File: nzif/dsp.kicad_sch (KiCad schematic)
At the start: 64 parts, among them Q501 STD2805T4, SW501 SW_SPST, SW502 SW_Push, U501 ADAU1467WBCPZ300, U502 25AA1024-I/MF, U503 ADM811TARTZ-REEL7

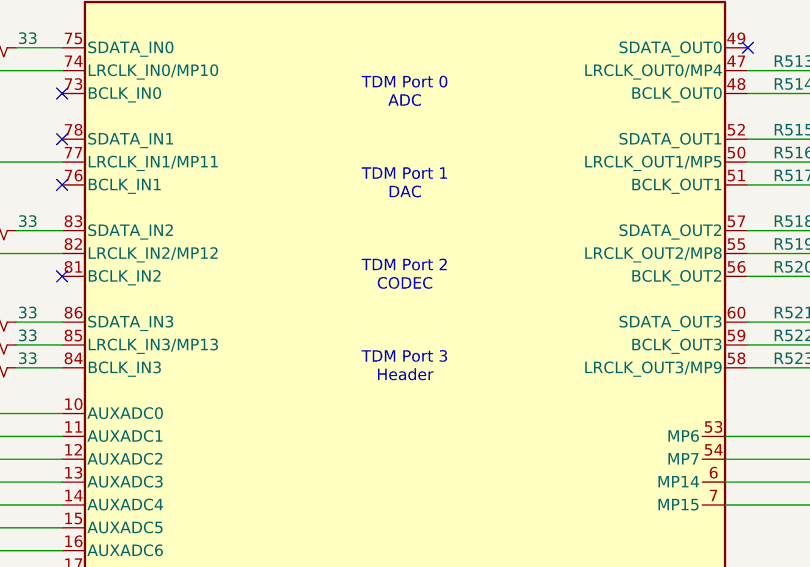
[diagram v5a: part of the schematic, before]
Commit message: top sheet wiring
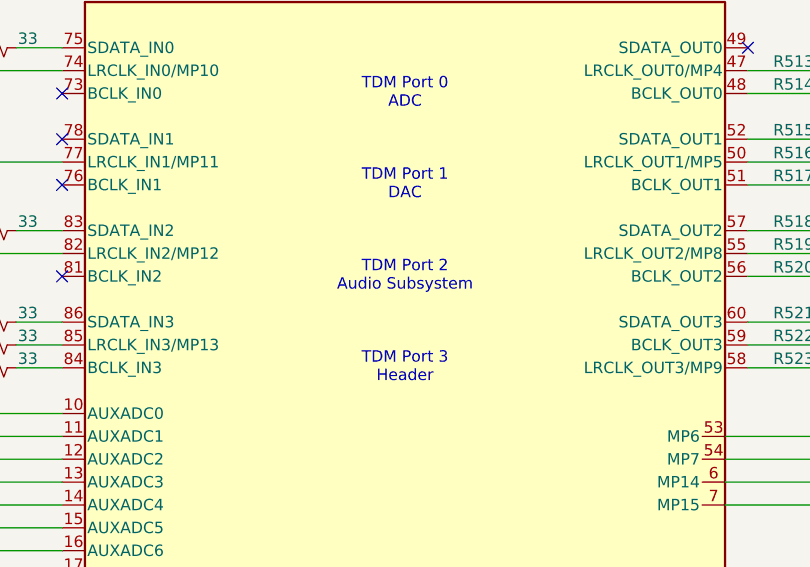
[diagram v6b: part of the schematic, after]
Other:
- note added: "TDM Port 2 Audio Subsystem"
- note removed: "TDM Port 2 CODEC"
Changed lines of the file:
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@@
 		)
 	)
-	(text "TDM Port 2\nCODEC"
+	(text "TDM Port 2\nAudio Subsystem"
 		(exclude_from_sim no)
 		(at 312.42 58.42 0)

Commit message: updates to top level
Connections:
- net DSP_MCLK: no longer names the net of U501.27 (CLKOUT)
- net MISO renamed SDA
- net MOSI renamed ADDR1
- net SCLK renamed SCL
- net SS renamed ADDR0
- no-connect marks 11 -> 12
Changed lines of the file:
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@@
+	)
+	(no_connect
+		(at 350.52 154.94)
 	)
 	(no_connect
@@
 	(wire
 		(pts
-			(xy 350.52 154.94) (xy 370.84 154.94)
-		)
-		(stroke
-			(width 0)
-			(type default)
-		)
-	)
-	(wire
-		(pts
 			(xy 363.22 55.88) (xy 370.84 55.88)
 		)
@@
 	)
 	(label "VDrive"
-		(at 266.7 152.4 180)
-		(effects
-			(font
-				(size 1.27 1.27)
-			)
-			(justify right bottom)
+		(at 266.7 152.4 0)
+		(effects
+			(font
+				(size 1.27 1.27)
+			)
+			(justify left bottom)
 		)
 	)
@@
 	)
 	(label "PLL_FILT"
-		(at 264.16 96.52 180)
-		(effects
-			(font
-				(size 1.27 1.27)
-			)
-			(justify right bottom)
+		(at 264.16 96.52 0)
+		(effects
+			(font
+				(size 1.27 1.27)
+			)
+			(justify left bottom)
 		)
 	)
@@
 	)
 	(label "MOSI_M"
-		(at 266.7 114.3 180)
-		(effects
-			(font
-				(size 1.27 1.27)
-			)
-			(justify right bottom)
+		(at 266.7 114.3 0)
+		(effects
+			(font
+				(size 1.27 1.27)
+			)
+			(justify left bottom)
 		)
 	)
 	(label "~{RESET}"
-		(at 264.16 99.06 180)
-		(effects
-			(font
-				(size 1.27 1.27)
-			)
-			(justify right bottom)
+		(at 264.16 99.06 0)
+		(effects
+			(font
+				(size 1.27 1.27)
+			)
+			(justify left bottom)
 		)
 	)
@@
 	)
 	(label "SCLK_M"
-		(at 266.7 119.38 180)
-		(effects
-			(font
-				(size 1.27 1.27)
-			)
-			(justify right bottom)
+		(at 266.7 119.38 0)
+		(effects
+			(font
+				(size 1.27 1.27)
+			)
+			(justify left bottom)
 		)
 	)
@@
 	)
 	(label "SELFBOOT"
-		(at 370.84 144.78 0)
-		(effects
-			(font
-				(size 1.27 1.27)
-			)
-			(justify left bottom)
+		(at 370.84 144.78 180)
+		(effects
+			(font
+				(size 1.27 1.27)
+			)
+			(justify right bottom)
 		)
 	)
@@
 	)
 	(label "SS_M"
-		(at 266.7 111.76 180)
-		(effects
-			(font
-				(size 1.27 1.27)
-			)
-			(justify right bottom)
+		(at 266.7 111.76 0)
+		(effects
+			(font
+				(size 1.27 1.27)
+			)
+			(justify left bottom)
 		)
 	)
@@
 	)
 	(label "MiSO_M"
-		(at 266.7 121.92 180)
-		(effects
-			(font
-				(size 1.27 1.27)
-			)
-			(justify right bottom)
+		(at 266.7 121.92 0)
+		(effects
+			(font
+				(size 1.27 1.27)
+			)
+			(justify left bottom)
 		)
 	)
@@
 		)
 	)
-	(hierarchical_label "MOSI"
+	(hierarchical_label "ADDR1"
 		(shape input)
 		(at 266.7 132.08 180)
@@
 		)
 	)
-	(hierarchical_label "SS"
+	(hierarchical_label "ADDR0"
 		(shape input)
 		(at 266.7 134.62 180)
@@
 		)
 	)
-	(hierarchical_label "MISO"
+	(hierarchical_label "SDA"
 		(shape output)
 		(at 266.7 127 180)
@@
 		)
 	)
-	(hierarchical_label "SCLK"
+	(hierarchical_label "SCL"
 		(shape input)
 		(at 266.7 129.54 180)
@@
 		(effects
 			(font
-				(size 1.27 1.27)
-			)
-			(justify left)
-		)
-	)
-	(hierarchical_label "DSP_MCLK"
-		(shape input)
-		(at 370.84 154.94 0)
-		(effects
-			(font

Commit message: updates to top level
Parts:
- added R1215: 49.9, symbol Device:R_Small_US
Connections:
- net MCLK: now also R1215.1; no longer U501.25 (XTALIN/MCLK)
- new net: R1215.2, U501.25 (XTALIN/MCLK)
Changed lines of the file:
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@@
 	(wire
 		(pts
+			(xy 256.54 160.02) (xy 261.62 160.02)
+		)
+		(stroke
+			(width 0)
+			(type default)
+		)
+	)
+	(wire
+		(pts
 			(xy 80.01 172.72) (xy 80.01 170.18)
 		)
@@
 	(hierarchical_label "MCLK"
 		(shape input)
-		(at 266.7 160.02 180)
+		(at 256.54 160.02 180)
 		(effects
 			(font
@@
 					(unit 1)
 				)
+			)
+		)
+	)
+	(symbol
+		(lib_id "Device:R_Small_US")
+		(at 264.16 160.02 90)
+		(unit 1)
+		(body_style 1)
+		(exclude_from_sim no)
+		(in_bom yes)
+		(on_board yes)
+		(in_pos_files yes)
+		(dnp no)
+		(fields_autoplaced yes)
+		(property "Reference" "R1215"
+			(at 264.16 153.67 90)
+			(show_name no)
+			(do_not_autoplace no)
+			(effects
+				(font
+					(size 1.27 1.27)
+				)
+			)
+		)
+		(property "Value" "49.9"
+			(at 264.16 156.21 90)
+			(show_name no)
+			(do_not_autoplace no)
+			(effects
+				(font
+					(size 1.27 1.27)
+				)
+			)
+		)
+		(property "Footprint" ""
+			(at 264.16 160.02 0)
+			(hide yes)
+			(show_name no)
+			(do_not_autoplace no)
+			(effects
+				(font
+					(size 1.27 1.27)
+				)
+			)
+		)
+		(property "Datasheet" ""
+			(at 264.16 160.02 0)
+			(hide yes)
+			(show_name no)
+			(do_not_autoplace no)
+			(effects
+				(font
+					(size 1.27 1.27)
+				)
+			)
+		)
+		(property "Description" "Resistor, small US symbol"
+			(at 264.16 160.02 0)
+			(hide yes)
+			(show_name no)
+			(do_not_autoplace no)
+			(effects
+				(font
+					(size 1.27 1.27)
+				)
+			)
+		)
+		(pin "1"
+		)
+		(pin "2"
+		)
+		(instances
+			(project "nzif"
+				(path "/fe42ca2f-2bb8-4d5a-9e84-807788ed632f/fa60d9db-5fbc-4f32-9a00-e3130bb41db9"
+					(reference "R1215")
+					(unit 1)
+				)
